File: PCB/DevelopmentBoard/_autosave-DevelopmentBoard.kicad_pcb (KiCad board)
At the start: 2 copper layers, 152.4 x 76.2 mm, 19 parts

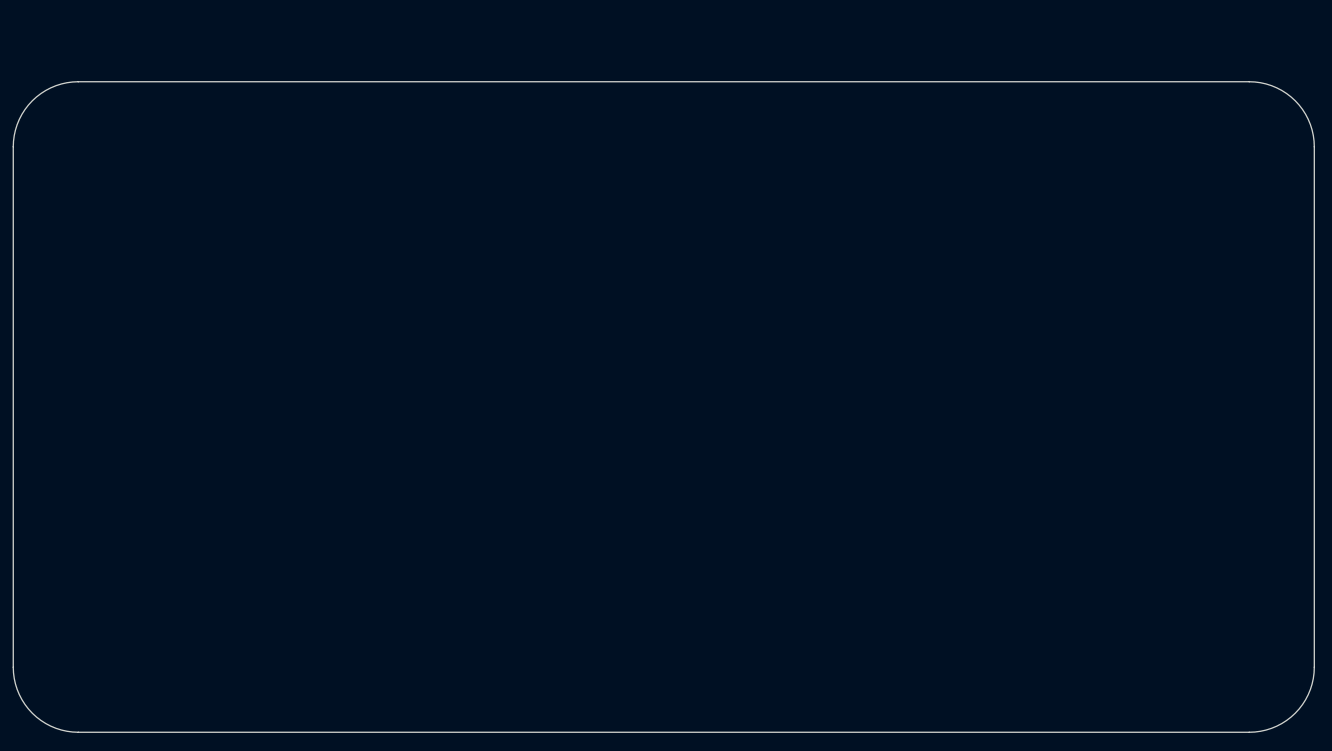
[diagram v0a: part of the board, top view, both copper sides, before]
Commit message: Created new footprints for components and setup a rough draft of component placements on board
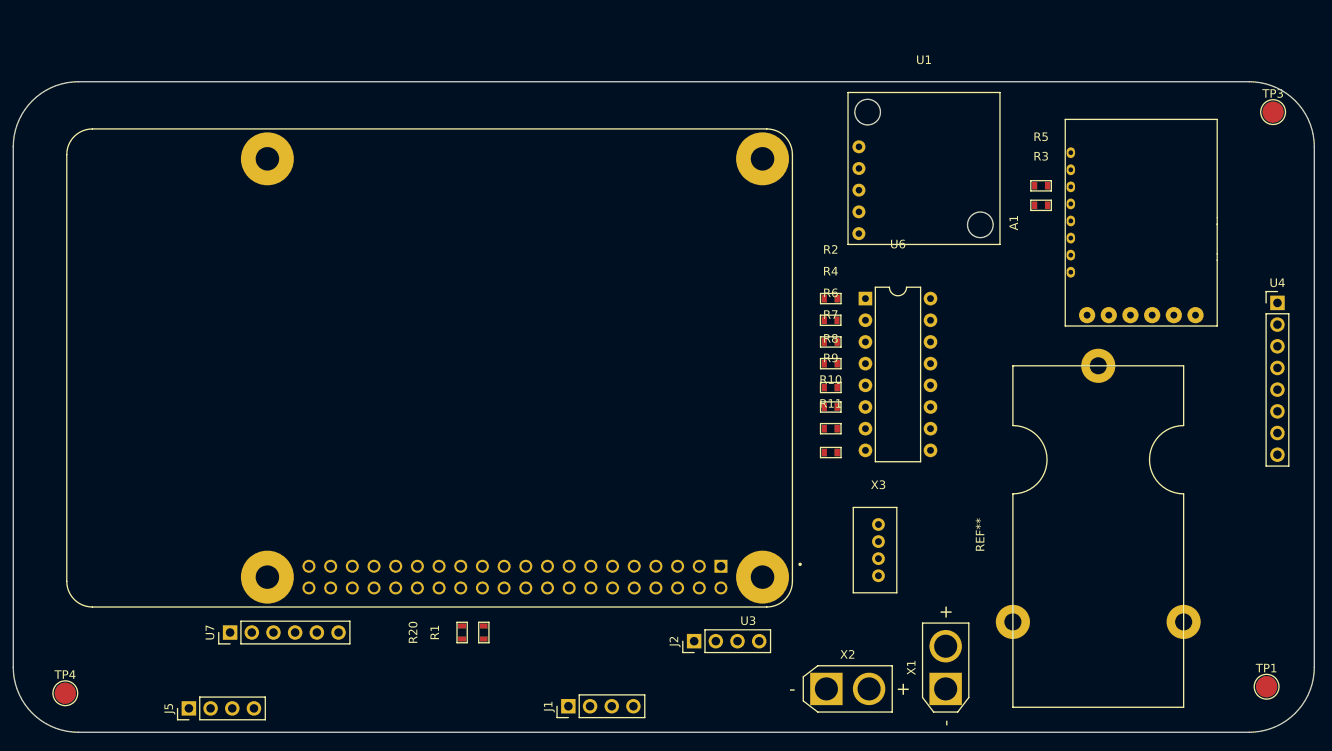
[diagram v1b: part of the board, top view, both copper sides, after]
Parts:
- added A1: TBS_Crossfire_RF, DevelopmentBoard:TBS_Crossfire_RF, F.Cu at (204.5, 79.0)
- added J1: Conn_01x04_MountingPin, Connector_PinHeader_2.54mm:PinHeader_1x04_P2.54mm_Vertical, F.Cu at (137.7, 135.6)
- added J2: Conn_01x04_MountingPin-PayloadSymbols, Connector_PinHeader_2.54mm:PinHeader_1x04_P2.54mm_Vertical, F.Cu at (152.5, 128.0)
- added J5: Conn_01x04_MountingPin, Connector_PinHeader_2.54mm:PinHeader_1x04_P2.54mm_Vertical, F.Cu at (93.3, 135.9)
- added R1: 4.7k, DevelopmentBoard:0603, F.Cu at (127.8, 127.0)
- added R10: 0, DevelopmentBoard:0603, F.Cu at (168.5, 103.1)
- added R11: 0, DevelopmentBoard:0603, F.Cu at (168.5, 105.9)
- added R2: 0, DevelopmentBoard:0603, F.Cu at (168.5, 87.8)
- added R20: 4.7k, DevelopmentBoard:0603, F.Cu at (125.3, 127.0)
- added R3: 4.7k, DevelopmentBoard:0603, F.Cu at (193.1, 76.9)
- added R4: 0, DevelopmentBoard:0603, F.Cu at (168.5, 90.4)
- added R5: 4.7k, DevelopmentBoard:0603, F.Cu at (193.1, 74.6)
- added R6: 0, DevelopmentBoard:0603, F.Cu at (168.5, 92.9)
- added R7: 0, DevelopmentBoard:0603, F.Cu at (168.5, 95.5)
- added R8: 0, DevelopmentBoard:0603, F.Cu at (168.5, 98.3)
- added R9: 0, DevelopmentBoard:0603, F.Cu at (168.5, 100.5)
- added REF**: Barometer_Grove, DevelopmentBoard:Barometer_Grove, F.Cu at (189.8, 95.7)
- added TP1: TestPoint, TestPoint:TestPoint_Pad_D2.5mm, F.Cu at (219.5, 133.3)
- added TP3: TestPoint, TestPoint:TestPoint_Pad_D2.5mm, F.Cu at (220.3, 66.0)
- added TP4: TestPoint, TestPoint:TestPoint_Pad_D2.5mm, F.Cu at (78.8, 134.1)
- added U1: D24V22F5_VoltageRegulator, DevelopmentBoard:D24V22F5_VoltageRegulator, F.Cu at (179.4, 72.6)
- added U3: RASPBERRY_PI_3_MODEL_B+, DevelopmentBoard:MODULE_RASPBERRY_PI_3_MODEL_B+, F.Cu at (121.5, 96.0)
- added U4: Conn_01x08_DevBoardSymbols, Connector_PinHeader_2.54mm:PinHeader_1x08_P2.54mm_Vertical, F.Cu at (220.8, 88.4)
- added U6: MCP3008_ADC, DevelopmentBoard:MCP3008_ADC, F.Cu at (176.3, 109.4)
- added U7: Conn_01x06_DevBoard_Symbols, Connector_PinHeader_2.54mm:PinHeader_1x06_P2.54mm_Vertical, F.Cu at (98.1, 127.0)
- added X1: XT30, Connector_AMASS:AMASS_XT30U-M_1x02_P5.0mm_Vertical, F.Cu at (181.9, 133.6)
- added X2: XT30, Connector_AMASS:AMASS_XT30U-M_1x02_P5.0mm_Vertical, F.Cu at (168.0, 133.6)
- added X3: 2mmGrove_Connector, DevelopmentBoard:2mmGrove_Connector, F.Cu at (174.1, 117.3)
